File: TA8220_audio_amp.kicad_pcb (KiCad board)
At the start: 2 copper layers, 50 x 52.2 mm, 24 parts, among them J1 Input, J2 Output, J3 Power

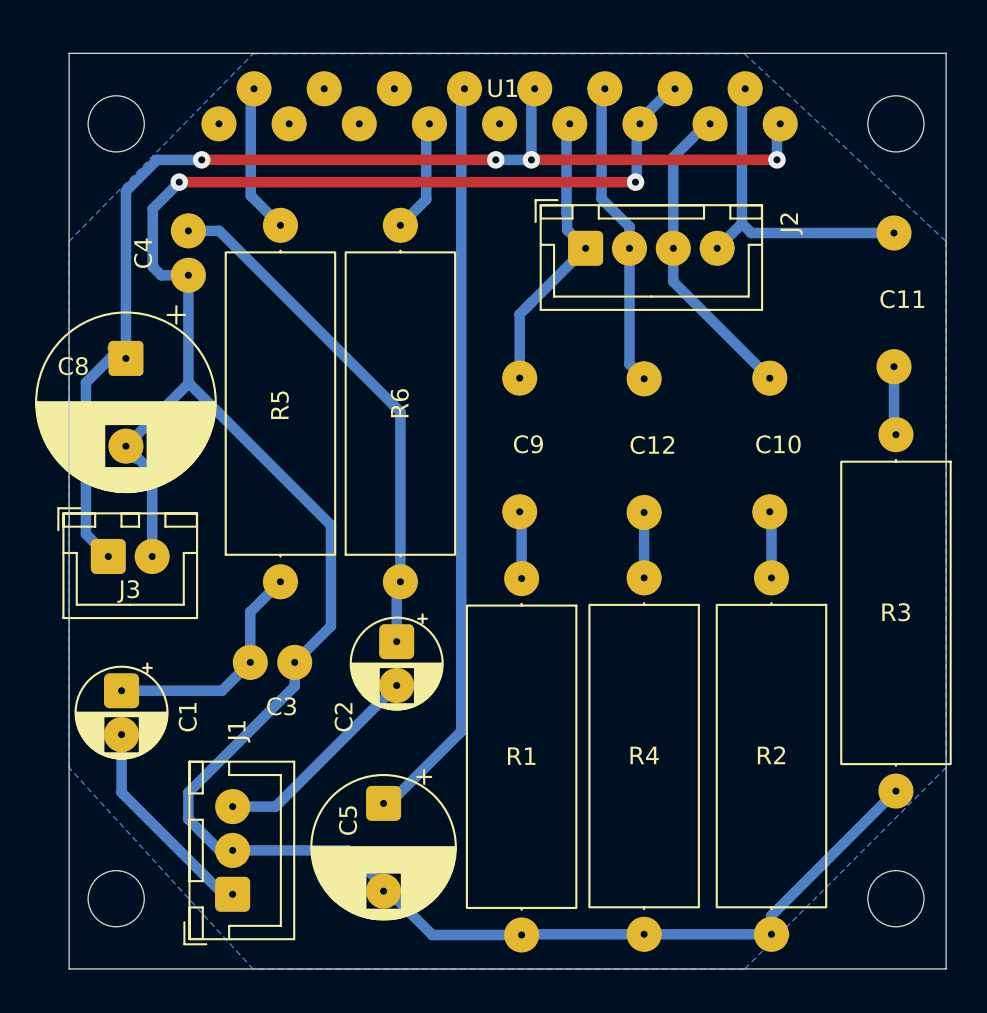
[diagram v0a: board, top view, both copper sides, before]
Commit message: ジャンパのパッドの大きさを修正
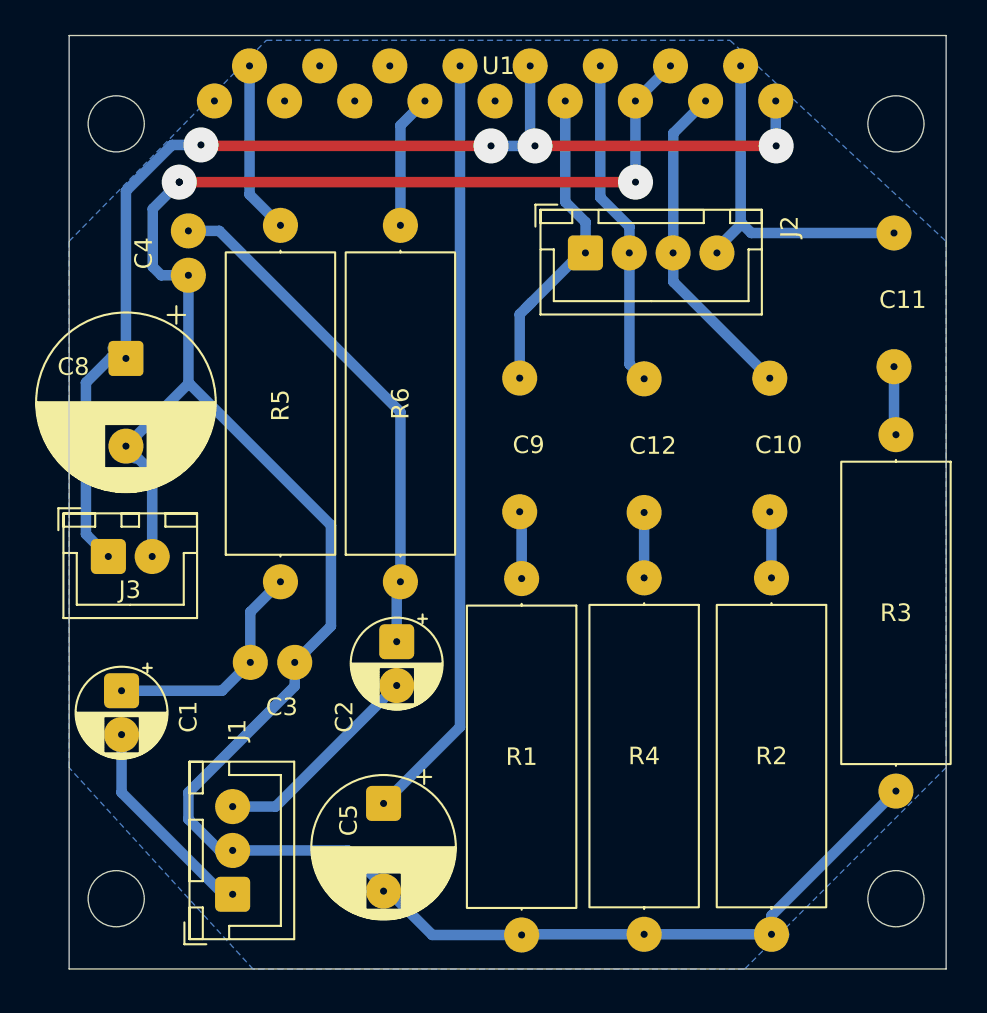
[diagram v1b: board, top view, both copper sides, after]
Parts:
- moved U1 1.33 mm to (163.8, 35.0)
- moved J2 0.26 mm to (168.9, 43.7)
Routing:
- net GND: track 138.4 -> 139.9 mm, vias 2 -> 3
- net VCC: track 67.3 -> 68.8 mm
- net Net-(U1-Ripple): track 42.5 -> 43.9 mm
- net Net-(U1-IN1): track 8.50 -> 9.82 mm
- net Net-(J2-Pin_4): track 18.6 -> 19.9 mm
- net Net-(J2-Pin_2): track 18.4 -> 19.7 mm
- net Net-(J2-Pin_1): track 16.9 -> 18.2 mm
- net Net-(U1-IN2): track 6.41 -> 7.67 mm
- net Net-(J2-Pin_3): track 17.6 -> 18.8 mm
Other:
- board size 50 x 52.2 mm -> 50 x 53.2 mm

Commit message: データシートどおりに作り直し
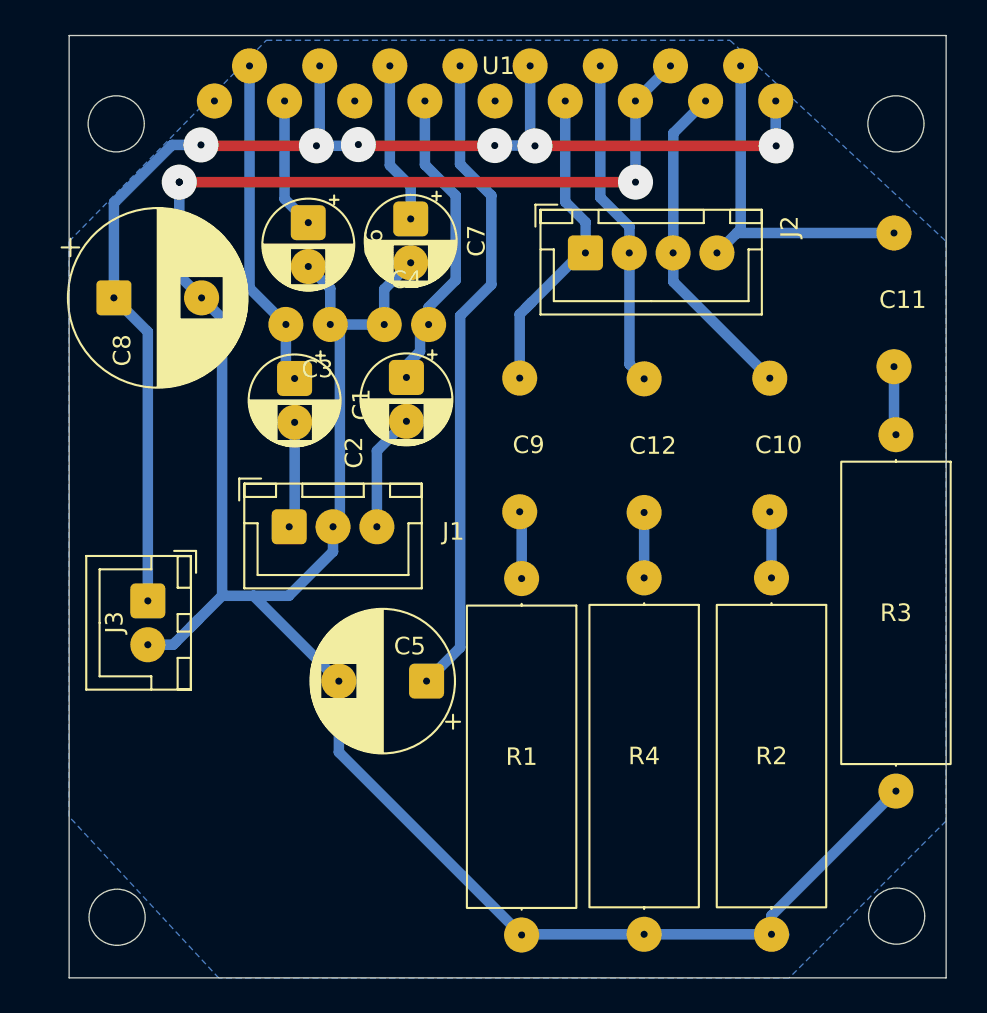
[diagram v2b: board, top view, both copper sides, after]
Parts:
- removed R5, R6: 18k, Resistor_THT:R_Axial_DIN0617_L17.0mm_D6.0mm_P20.32mm_Horizontal
- added C6: 25v47uF, Capacitor_THT:CP_Radial_D5.0mm_P2.50mm, F.Cu at (153.1, 41.9)
- added C7: 25v47uF, Capacitor_THT:CP_Radial_D5.0mm_P2.50mm, F.Cu at (159.0, 41.7)
- moved J1 21.2 mm to (152.1, 59.3), turned to 0 degrees
- moved C1 20.4 mm to (152.4, 50.8)
- moved C3 19.4 mm to (153.1, 47.7)
- moved C2 15.1 mm to (158.7, 50.8)
- moved C4 13.1 mm to (158.7, 47.7), turned to 180 degrees
- moved C5 7.39 mm to (159.9, 68.1), turned to 180 degrees
- moved C8 3.52 mm to (142.1, 46.2), turned to 0 degrees
- moved J3 3.39 mm to (144.0, 63.5), turned to -90 degrees
- moved H3 1.06 mm to (142.2, 81.5)
- moved H4 0.99 mm to (186.7, 81.5)
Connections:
- C1 pad 1: Net-(C1-Pad1) -> Net-(U1-IN1)
- C2 pad 1: Net-(C2-Pad1) -> Net-(U1-IN2)
- C3 pad 1: Net-(C1-Pad1) -> Net-(U1-IN1)
- C4 pad 1: Net-(C2-Pad1) -> Net-(U1-IN2)
- U1 pad 3: unconnected-(U1-NF1-Pad3) -> Net-(U1-NF1)
- U1 pad 4: unconnected-(U1-Stand-by_SW-Pad4) -> VCC
- U1 pad 6: unconnected-(U1-NF2-Pad6) -> Net-(U1-NF2)
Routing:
- net Net-(C2-Pad1): track 29.5 -> 0.00 mm
- net Net-(C1-Pad1): track 13.3 -> 0.00 mm
- net Net-(U1-IN2): track 7.67 -> 17.7 mm
- net Net-(U1-NF2): track 0.00 -> 9.22 mm
- net Net-(U1-IN1): track 9.82 -> 18.9 mm
- net GND: track 139.9 -> 148.6 mm
- net Net-(U1-NF1): track 0.00 -> 7.50 mm
- net Net-(U1-Ripple): track 43.9 -> 37.3 mm
- net Net-(J1-Pin_1): track 12.0 -> 6.08 mm
- net VCC: track 68.8 -> 74.5 mm, vias 4 -> 6
- net Net-(J1-Pin_3): track 12.2 -> 6.71 mm
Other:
- board size 50 x 53.2 mm -> 50 x 53.7 mm
